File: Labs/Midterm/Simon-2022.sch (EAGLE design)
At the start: 19 parts

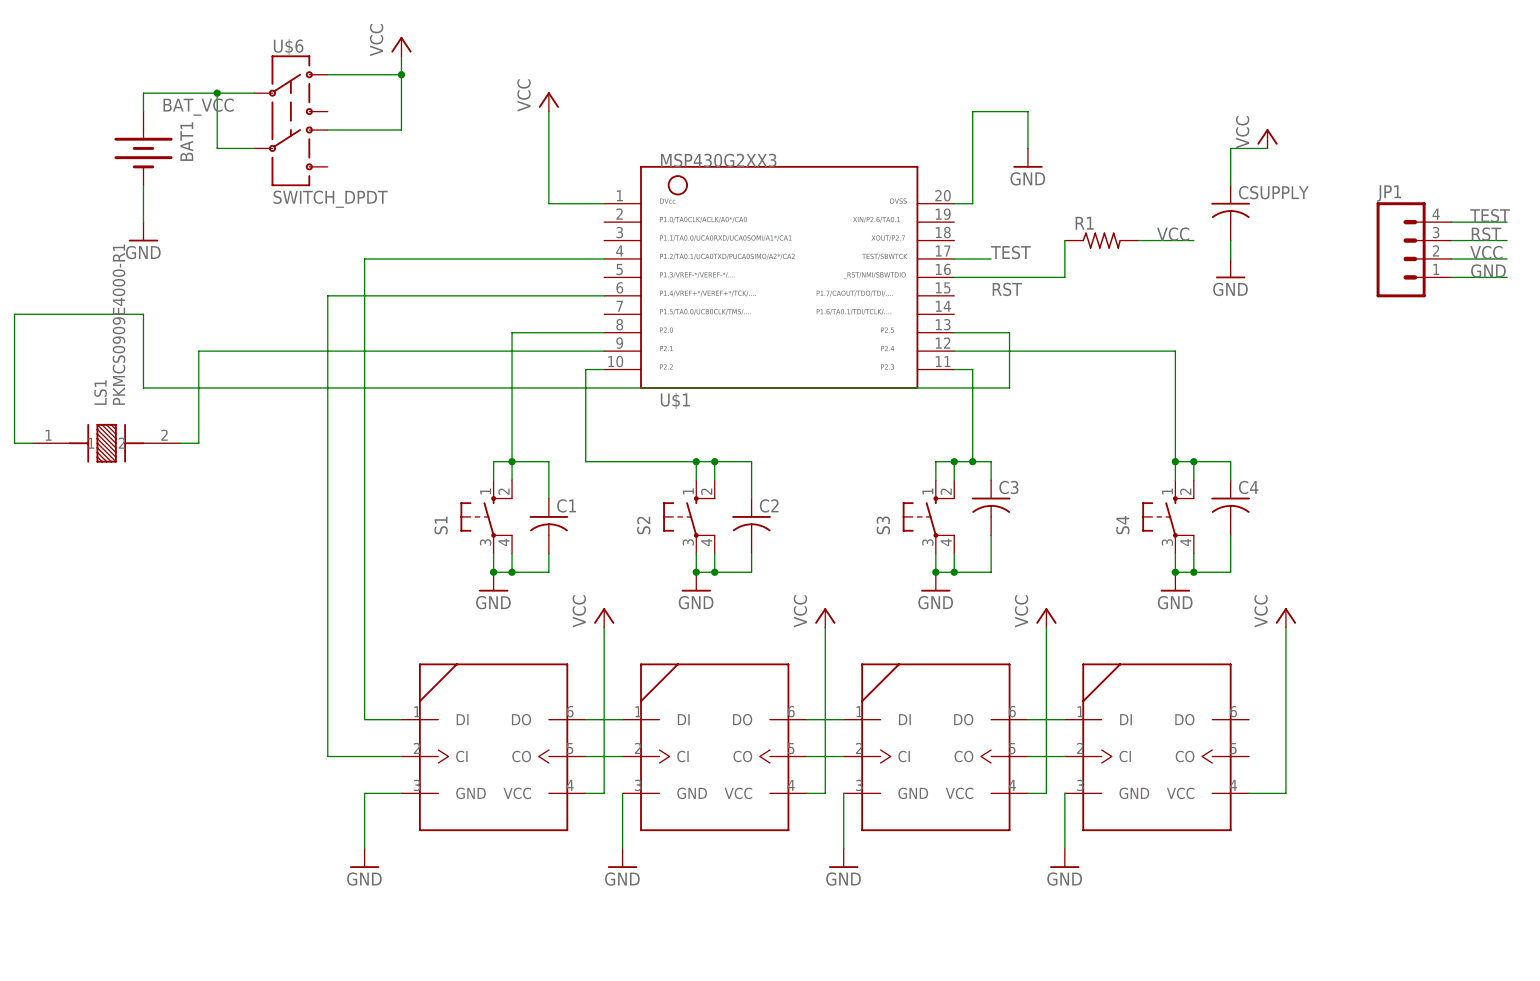
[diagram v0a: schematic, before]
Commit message: Added FR examples
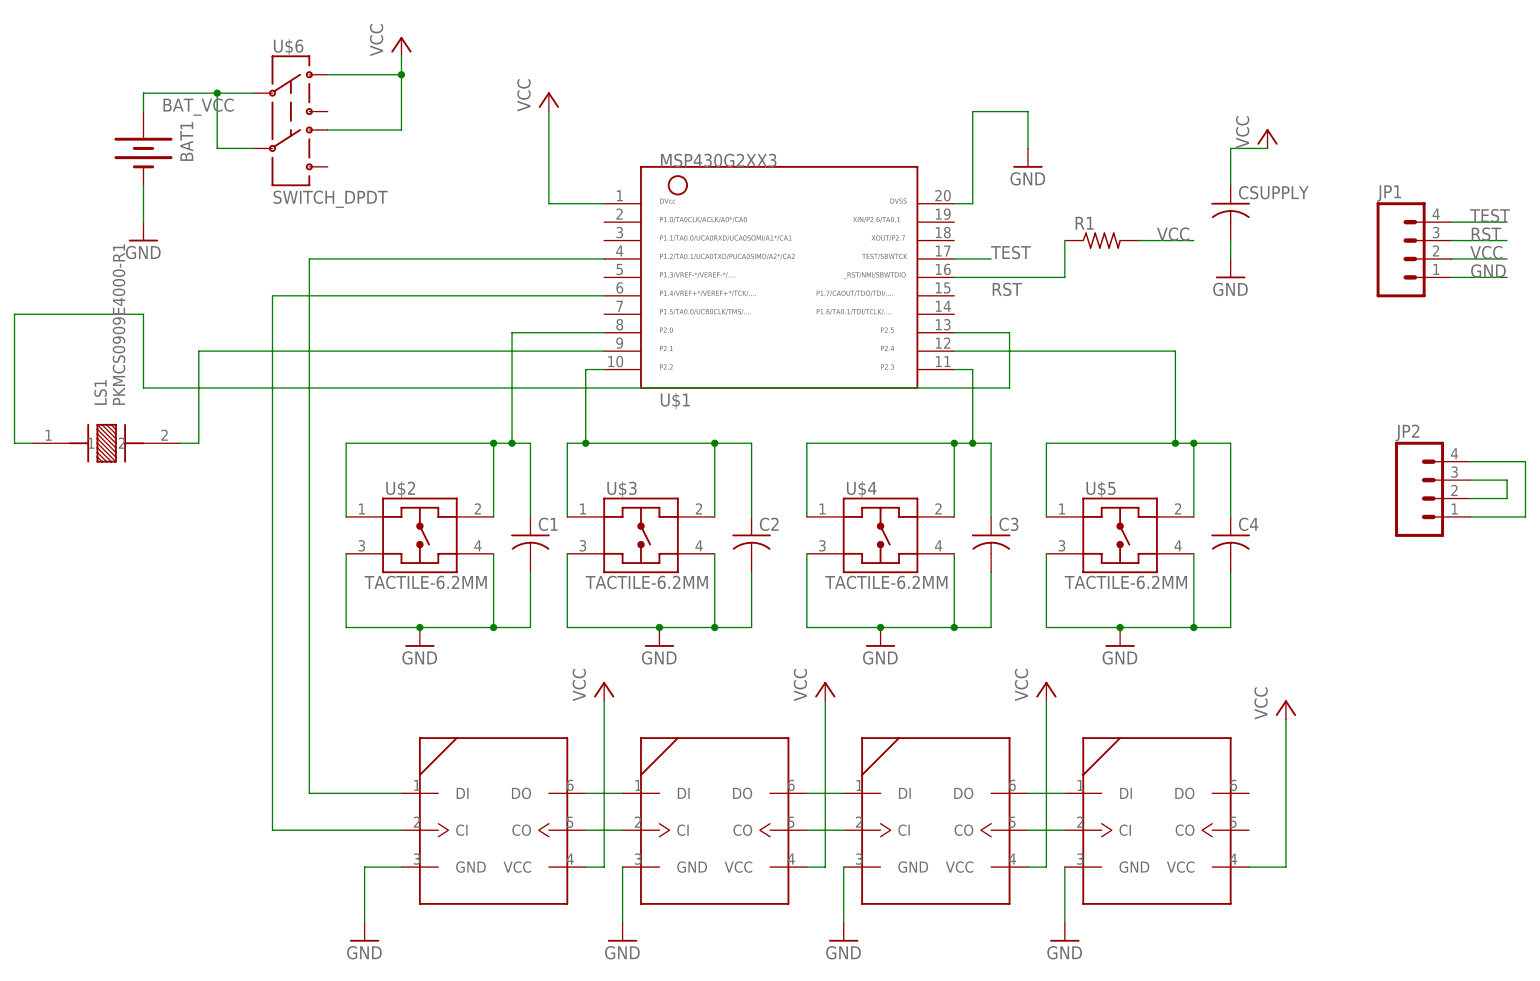
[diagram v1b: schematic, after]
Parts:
- removed S1, S2, S3, S4: (no value), switch-omron:10-XX
- added JP2: (no value), SparkFun:M04LOCK
- added U$2, U$3, U$4, U$5: TACTILE-6.2MM, ELEC327:TACTILE-6.2MM
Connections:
- removed net N$15: C3.1, S3.S, S3.S1, U$1.11
- new net N$12: C1.1, U$1.8, U$2.1, U$2.3
- new net N$20: C4.1, U$1.12, U$5.1, U$5.3
- new net N$9: C2.1, U$1.10, U$3.1, U$3.3
- net GND: now also U$2.2, U$2.4, U$3.2, U$3.4, U$4.2, U$4.4, U$5.2, U$5.4; no longer S1.P, S1.P1, S2.P, S2.P1, S3.P, S3.P1, S4.P, S4.P1
- net N$13: now also JP2.1, JP2.4; no longer C1.1, S1.S, S1.S1, U$1.8
- net N$14: now also JP2.2, JP2.3; no longer C2.1, S2.S, S2.S1, U$1.10
- net N$16: now also C3.1, U$1.11, U$4.1, U$4.3; no longer C4.1, S4.S, S4.S1, U$1.12
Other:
- moved on the sheet: C1, C2, C3, C4
